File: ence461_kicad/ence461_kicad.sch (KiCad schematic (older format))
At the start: 64 parts, among them J1 Conn_02x05_Odd_Even, Q1 Q_PMOS_GSD, U1 LMV324, U2 LMV324, U3 LMV324, U4 74HC3G14DP, U5 LMV321, U6 NCV7344D13R2GOSCT-ND, U7 MIC5202, U9 MKE16Z32VLD4

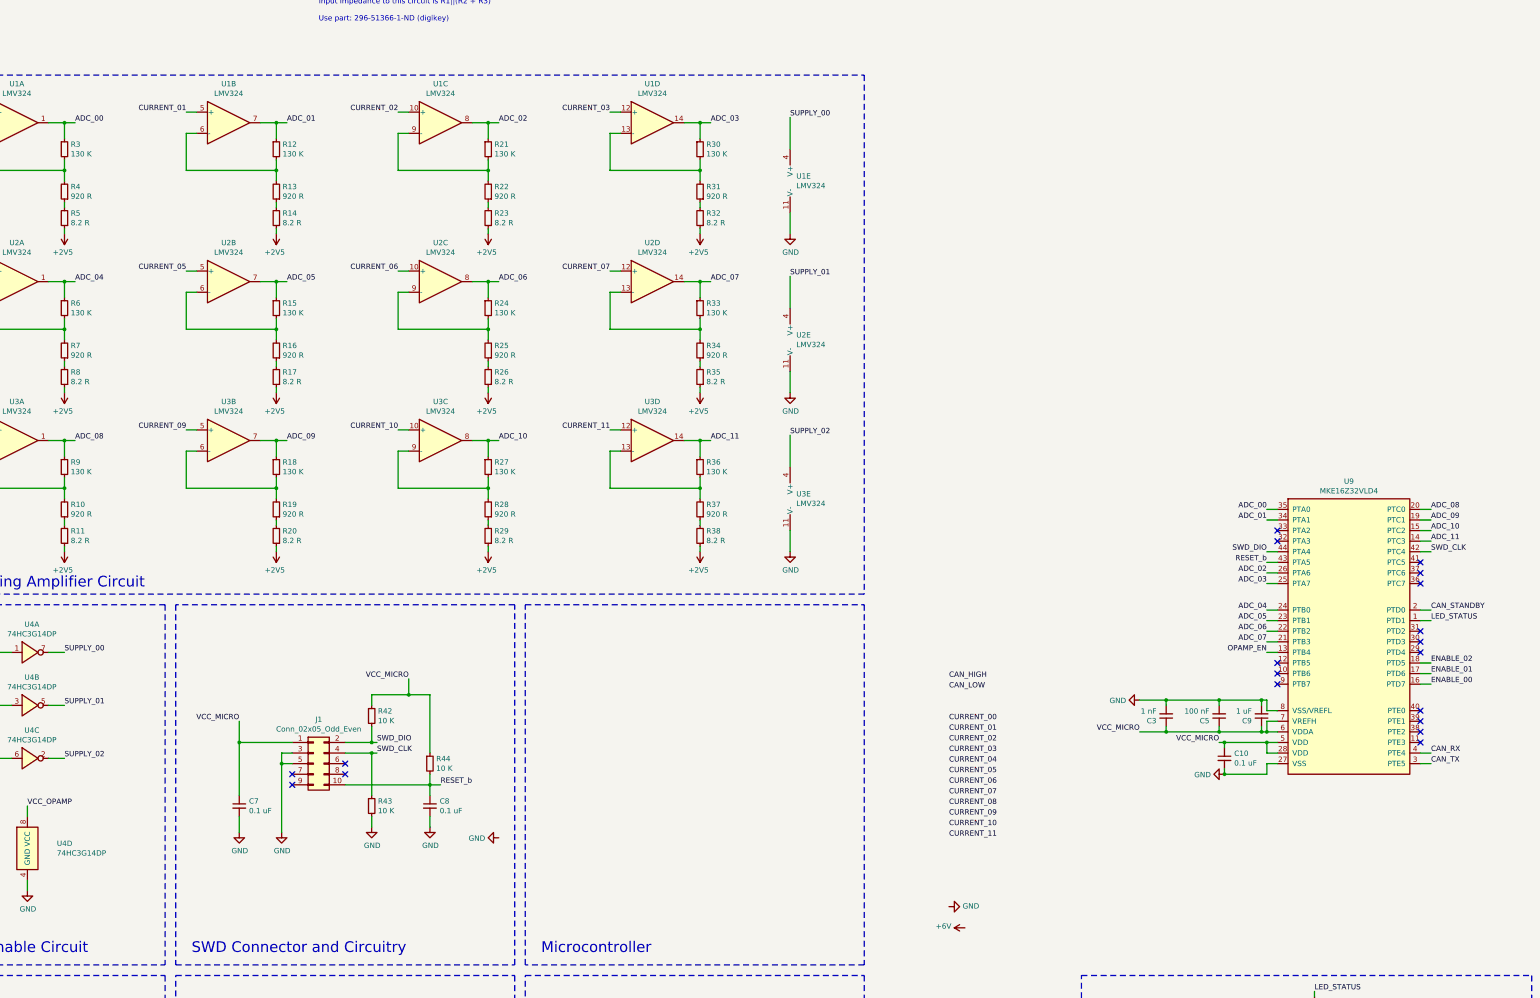
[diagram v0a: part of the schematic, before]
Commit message: Added RC filtering.
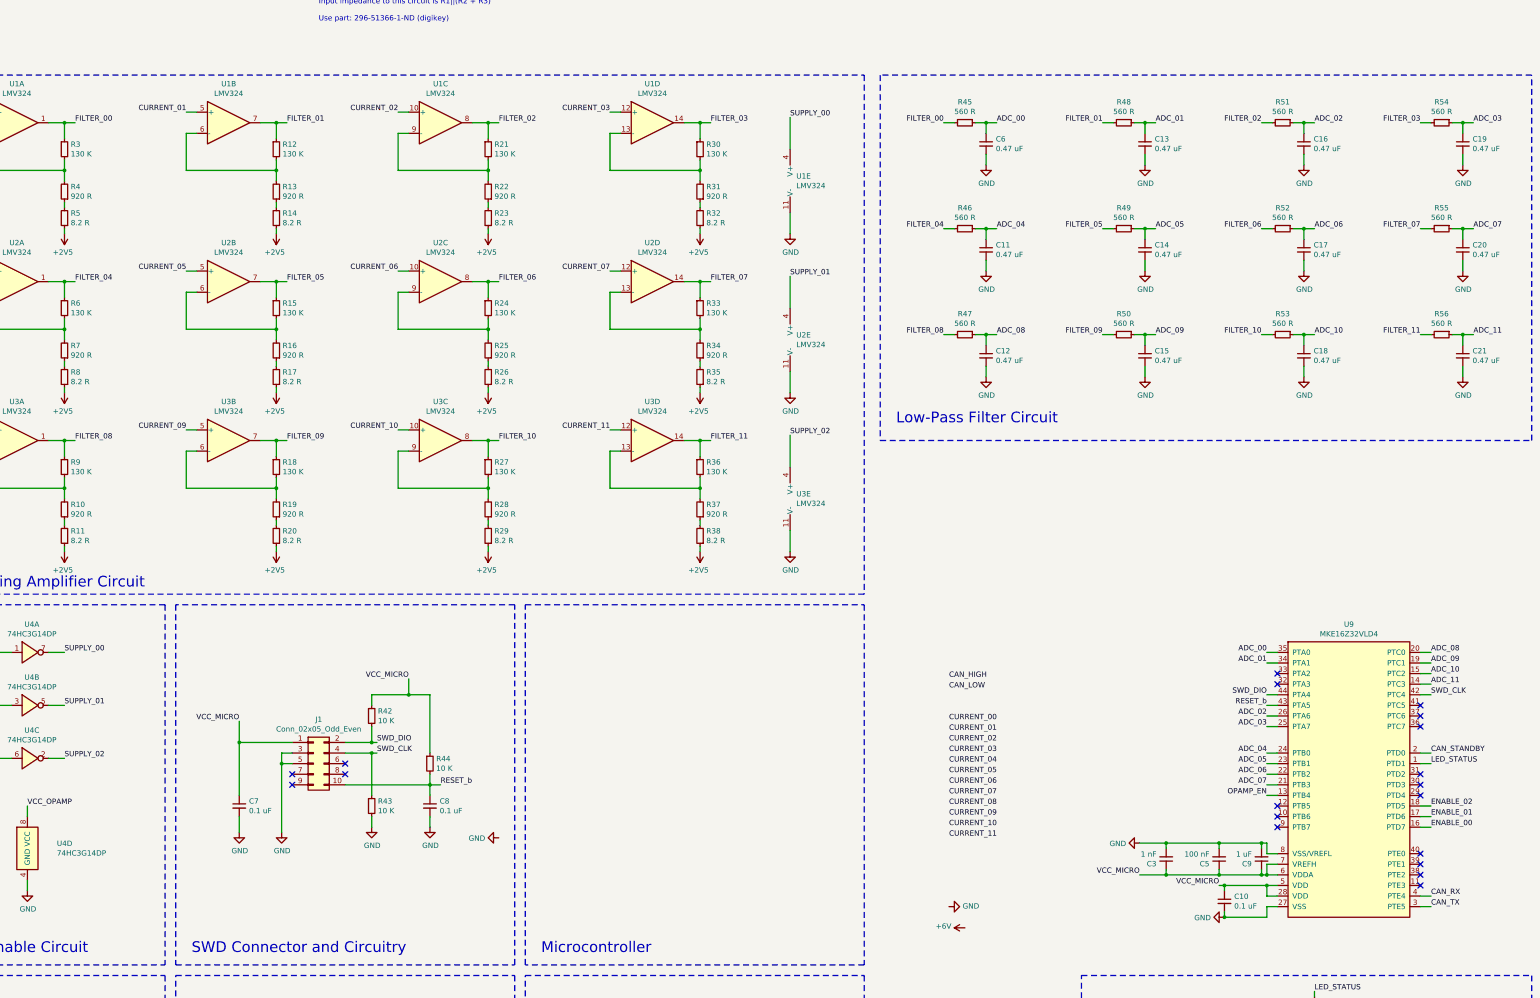
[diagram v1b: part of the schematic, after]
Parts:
- added C11, C12, C13, C14, C15, C16, C17, C18, C19, C20, C21, C6: 0.47 uF, Capacitor_SMD:C_0402_1005Metric, symbol Device:C_Small
- added R45, R46, R47, R48, R49, R50, R51, R52, R53, R54, R55, R56: 560 R, Resistor_SMD:R_0402_1005Metric, symbol Device:R_Small
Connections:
- net ADC_00: now also C6.1, R45.1; no longer R3.1, U1.1
- net ADC_01: now also C13.1, R48.1; no longer R12.1, U1.7
- net ADC_02: now also C16.1, R51.1; no longer R21.1, U1.8
- net ADC_03: now also C19.1, R54.1; no longer R30.1, U1.14
- net ADC_04: now also C11.1, R46.1; no longer R6.1, U2.1
- net ADC_05: now also C14.1, R49.1; no longer R15.1, U2.7
- net ADC_06: now also C17.1, R52.1; no longer R24.1, U2.8
- net ADC_07: now also C20.1, R55.1; no longer R33.1, U2.14
- net ADC_08: now also C12.1, R47.1; no longer R9.1, U3.1
- net ADC_09: now also C15.1, R50.1; no longer R18.1, U3.7
- net ADC_10: now also C18.1, R53.1; no longer R27.1, U3.8
- net ADC_11: now also C21.1, R56.1; no longer R36.1, U3.14
- net GND: now also C11.2, C12.2, C13.2, C14.2, C15.2, C16.2, C17.2, C18.2, C19.2, C20.2, C21.2, C6.2
- new net FILTER_00: R3.1, R45.2, U1.1
- new net FILTER_01: R12.1, R48.2, U1.7
- new net FILTER_02: R21.1, R51.2, U1.8
- new net FILTER_03: R30.1, R54.2, U1.14
- new net FILTER_04: R46.2, R6.1, U2.1
- new net FILTER_05: R15.1, R49.2, U2.7
- new net FILTER_06: R24.1, R52.2, U2.8
- new net FILTER_07: R33.1, R55.2, U2.14
- new net FILTER_08: R47.2, R9.1, U3.1
- new net FILTER_09: R18.1, R50.2, U3.7
- new net FILTER_10: R27.1, R53.2, U3.8
- new net FILTER_11: R36.1, R56.2, U3.14
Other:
- note added: "Low-Pass Filter Circuit"
- moved on the sheet: C10, C3, C5, C9, U9

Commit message: Almost there!
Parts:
- added H1, H2, H3: MountingHole, MountingHole:MountingHole_3mm, symbol Mechanical:MountingHole
- added J2: INPUT_0, Connector_PinSocket_1.27mm:PinSocket_1x04_P1.27mm_Vertical, symbol Connector_Generic:Conn_01x04
- added J3: INPUT_1, Connector_PinSocket_1.27mm:PinSocket_1x04_P1.27mm_Vertical, symbol Connector_Generic:Conn_01x04
- added J4: CANBUS, Connector_PinHeader_1.27mm:PinHeader_2x05_P1.27mm_Vertical, symbol Connector_Generic:Conn_02x05_Odd_Even
- added J5: INPUT_2, Connector_PinSocket_1.27mm:PinSocket_1x04_P1.27mm_Vertical, symbol Connector_Generic:Conn_01x04
- added JP1: CAN_HIGH, Jumper:SolderJumper-3_P1.3mm_Open_Pad1.0x1.5mm, symbol Jumper:SolderJumper_3_Open
- added JP2: CAN_LOW, Jumper:SolderJumper-3_P1.3mm_Open_Pad1.0x1.5mm, symbol Jumper:SolderJumper_3_Open
- J1: value Conn_02x05_Odd_Even -> SWD
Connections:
- net CAN_HIGH: now also JP1.2 (C)
- net CAN_LOW: now also JP2.2 (C)
- net CURRENT_00: now also J2.1 (Pin_1)
- net CURRENT_01: now also J2.2 (Pin_2)
- net CURRENT_02: now also J2.3 (Pin_3)
- net CURRENT_03: now also J2.4 (Pin_4)
- net CURRENT_04: now also J3.1 (Pin_1)
- net CURRENT_05: now also J3.2 (Pin_2)
- net CURRENT_06: now also J3.3 (Pin_3)
- net CURRENT_07: now also J3.4 (Pin_4)
- net CURRENT_08: now also J5.1 (Pin_1)
- net CURRENT_09: now also J5.2 (Pin_2)
- net CURRENT_10: now also J5.3 (Pin_3)
- net CURRENT_11: now also J5.4 (Pin_4)
- new net CAN_HIGH_A: J4.4 (Pin_4), JP1.1 (A)
- new net CAN_HIGH_B: J4.7 (Pin_7), JP1.3 (B)
- new net CAN_LOW_A: J4.3 (Pin_3), JP2.1 (A)
- new net CAN_LOW_B: J4.8 (Pin_8), JP2.3 (B)
- no-connect marks 19 -> 25
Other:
- note added: "Current and Comms Connectors"
- note removed: "Microcontroller"
- moved on the sheet: C10, C3, C5, C9, U9

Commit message: Finished layout.
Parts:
- added J6: POWER, ence461_kicad:TB002-500, symbol Connector_Generic:Conn_01x02
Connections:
- net +6V: now also J6.1 (Pin_1)
- net GND: now also J6.2 (Pin_2)
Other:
- note added: "Microcontroller"
- note added: "Misc. Hardware"
- note removed: "Use a non-inverting amplifier circuit.\nThe gain is 1 + R1/(R2 + R3), where R1 is top resistor.\nNeed to use two resistors to achieve an accurate gain.\n\nInput impedance to this circuit is R1||(R2 + R3)\n\nUse part: 296-51366-1-ND (digikey)"
- note removed: "Use a virtual ground circuit.\n\nPart: 296-51364-1-ND (digikey)"
- moved on the sheet: C2, C3, C4, C5, C9, H1, H2, H3, U7
